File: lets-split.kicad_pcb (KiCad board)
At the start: 2 copper layers, 123.8 x 85.7 mm, 54 parts, among them J1 USB_C_Receptacle_USB2.0, SW1 Key_Tab, SW10 Key_D, SW11 Key_F, SW12 Key_G, SW13 Key_Shift, SW14 Key_Z, SW15 Key_X, SW16 Key_C, SW17 Key_V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

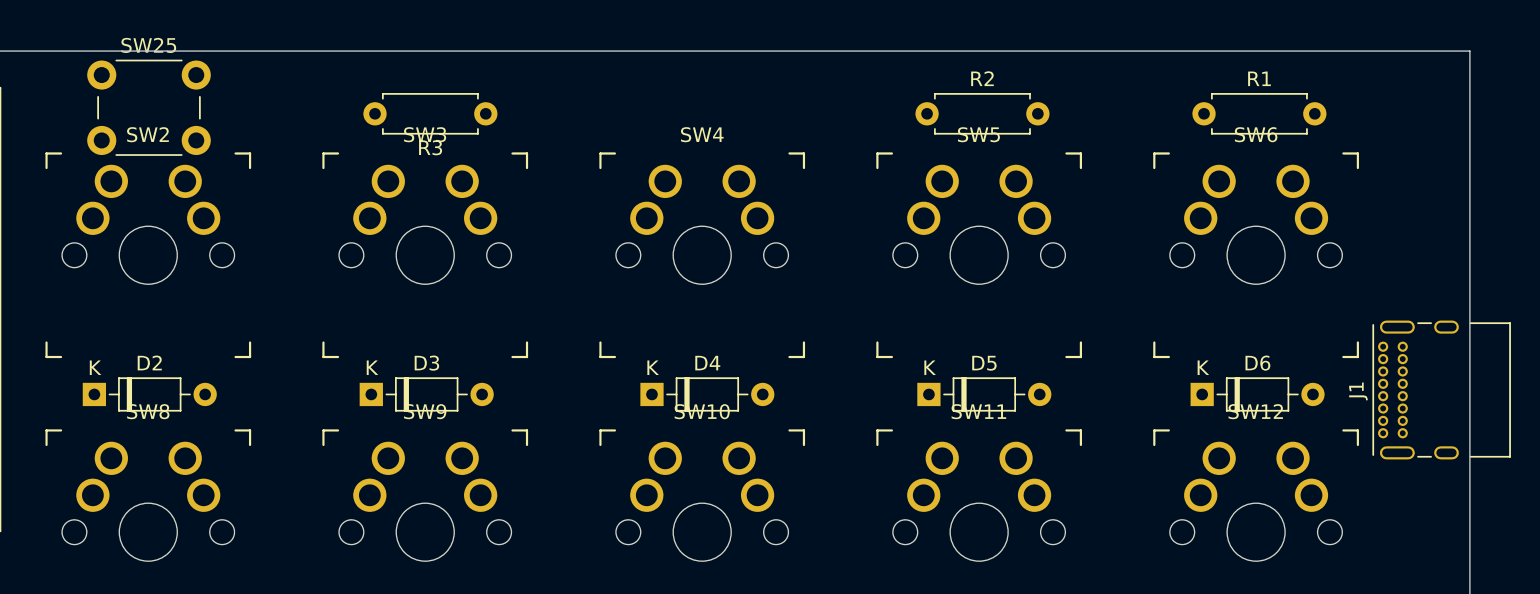
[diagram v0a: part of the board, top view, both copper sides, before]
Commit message: Fixed USB-C connector not passing inspection.
Added jumper to allow it to be mounted on either side of the board
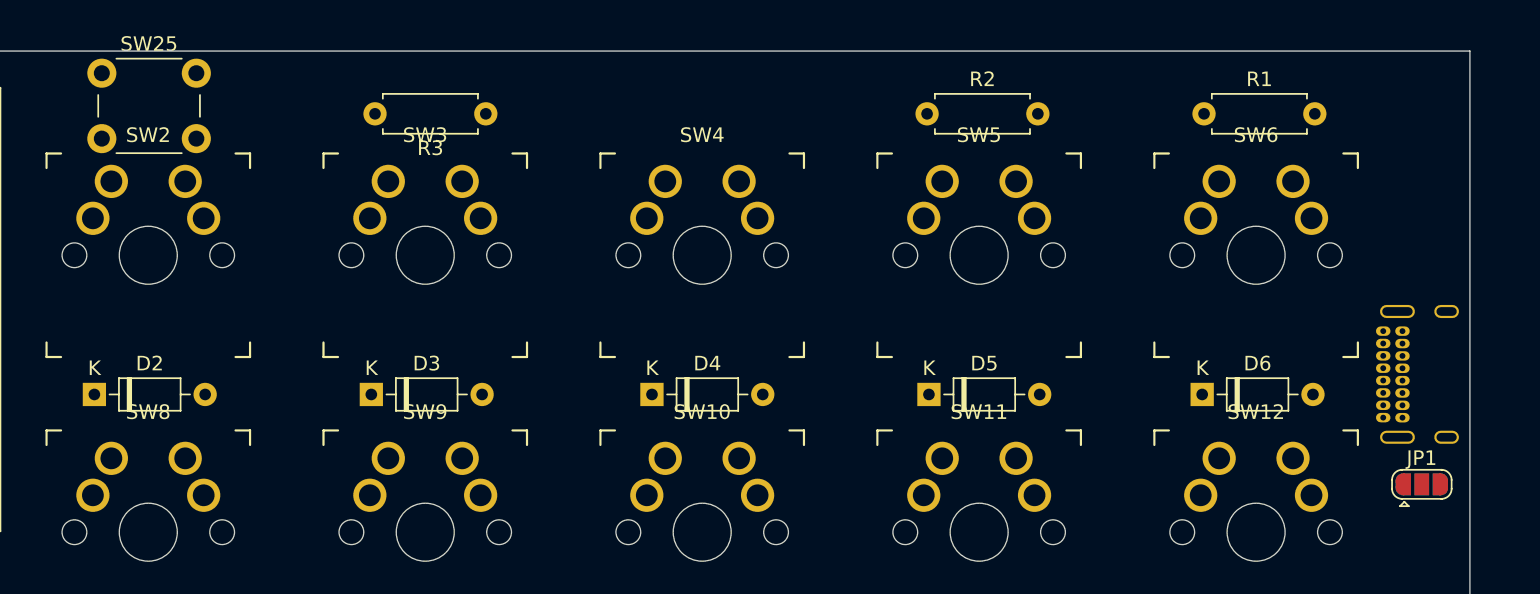
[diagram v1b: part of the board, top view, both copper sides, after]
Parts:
- added JP1: Jack Reversed Jumper, Jumper:SolderJumper-3_P1.3mm_Open_RoundedPad1.0x1.5mm, F.Cu at (196.7, 80.0)
- added JP2: Jack Obversed Jumper, Jumper:SolderJumper-3_P1.3mm_Open_RoundedPad1.0x1.5mm, B.Cu at (196.7, 80.0)
- J1: footprint Connector_USB:USB_C_Receptacle_GCT_USB4085 -> custom-footprints:USB_C_GCT_USB4085; moved to B.Cu
- moved J1 7.33 mm to (200.2, 72.4), turned to 270 degrees
- moved SW25 0.13 mm to (105.9, 51.7)
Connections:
- J1 pad B8: Net-(J1-PadA8) -> Net-(J1-PadB8)
- R3 pad 1: Net-(J1-PadA8) -> Net-(JP1-Pad1)

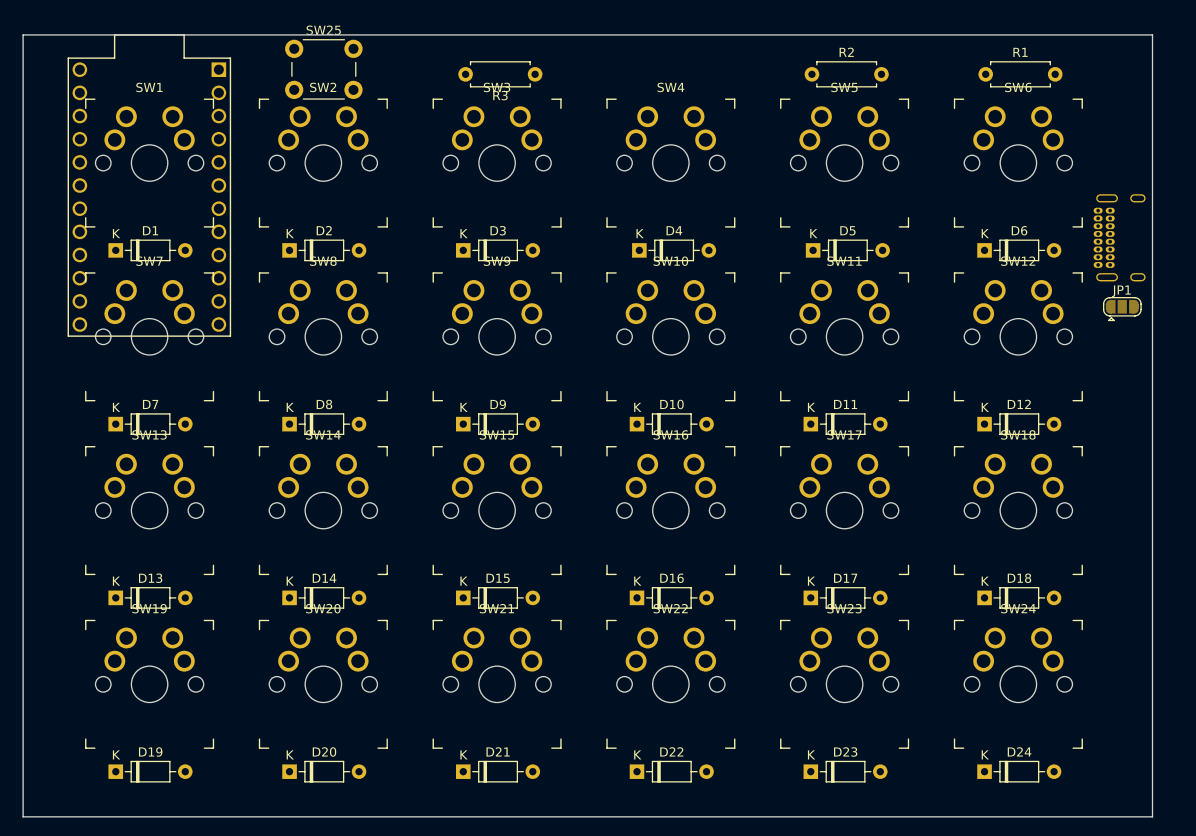
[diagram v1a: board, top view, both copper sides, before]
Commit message: PCB traces laid. Fixed labels on columns on schematic.
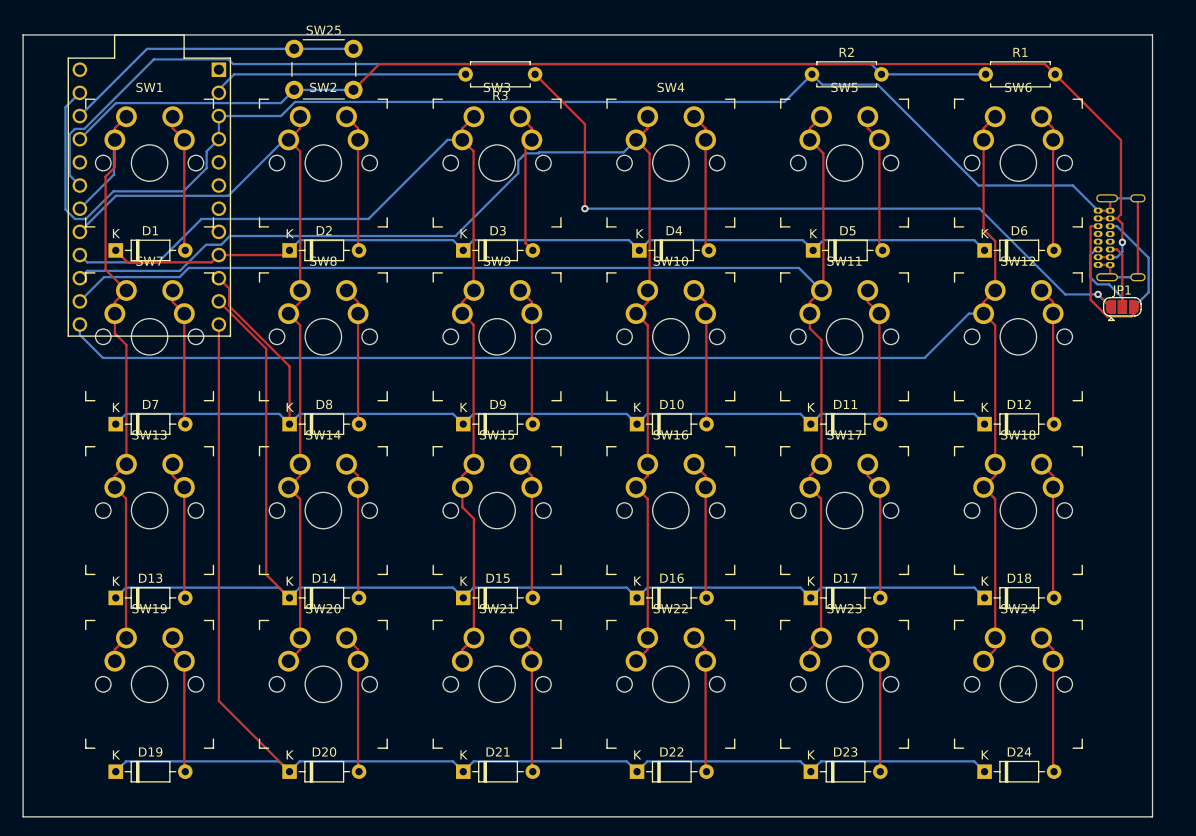
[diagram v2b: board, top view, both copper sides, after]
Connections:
- U1 pad 14: Col6 -> Col5
- U1 pad 15: Col6 -> Col4
- U1 pad 16: Col6 -> Col3
- U1 pad 17: Col6 -> Col2
- U1 pad 18: Col6 -> Col1
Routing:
- net Col6: track 0.00 -> 166.7 mm
- net GND: track 0.00 -> 163.5 mm
- net Row4: track 0.00 -> 152.1 mm
- net Col5: track 0.00 -> 147.4 mm
- net VCC: track 0.00 -> 138.7 mm, vias 0 -> 1
- net Row3: track 0.00 -> 135.6 mm
- net Col4: track 0.00 -> 131.6 mm
- net Row2: track 0.00 -> 119.1 mm
- net Col3: track 0.00 -> 111.2 mm
- net HalfSelector: track 0.00 -> 110.6 mm
- net Row1: track 0.00 -> 100.1 mm
- net Col2: track 0.00 -> 90.4 mm
- net Net-(JP1-Pad1): track 0.00 -> 81.0 mm, vias 0 -> 2
- net Col1: track 0.00 -> 73.4 mm
- net Reset: track 0.00 -> 33.1 mm
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
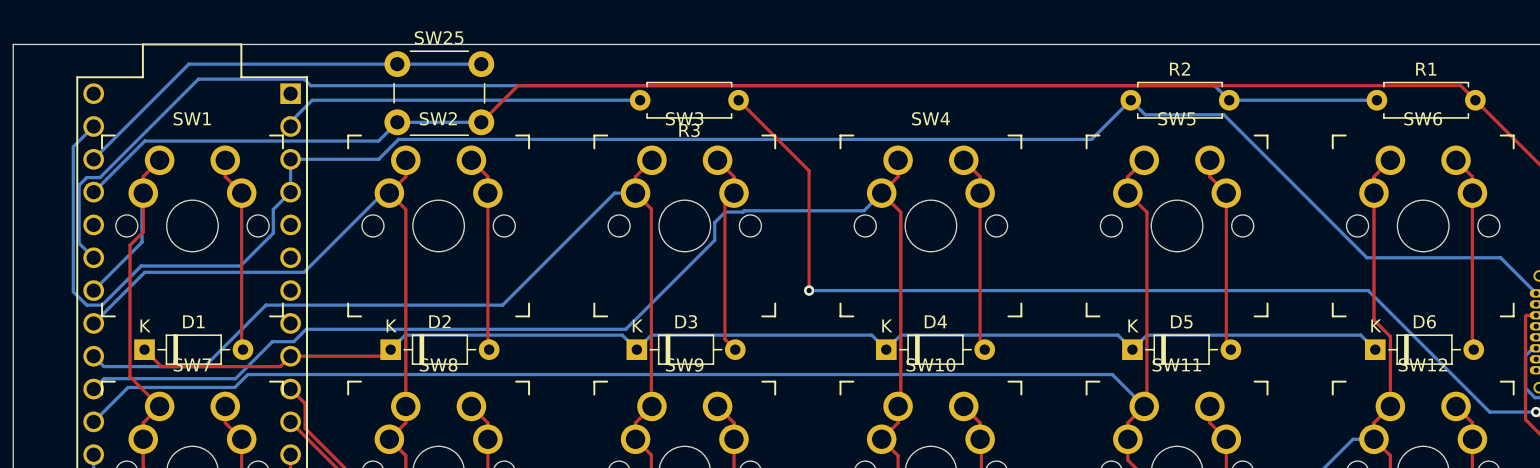
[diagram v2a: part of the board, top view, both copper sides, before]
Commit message: corrected reset button to go to gnd
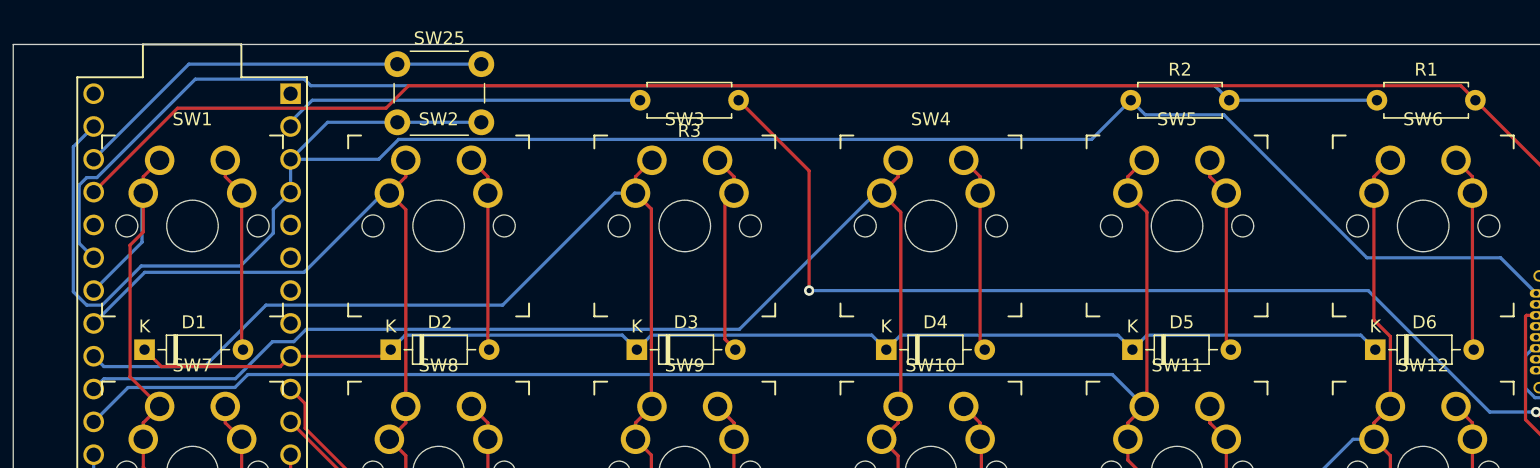
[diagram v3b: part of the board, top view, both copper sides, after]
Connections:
- SW25 pad 2: VCC -> GND
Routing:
- net GND: track 163.5 -> 179.4 mm
- net Col4: track 131.6 -> 130.8 mm

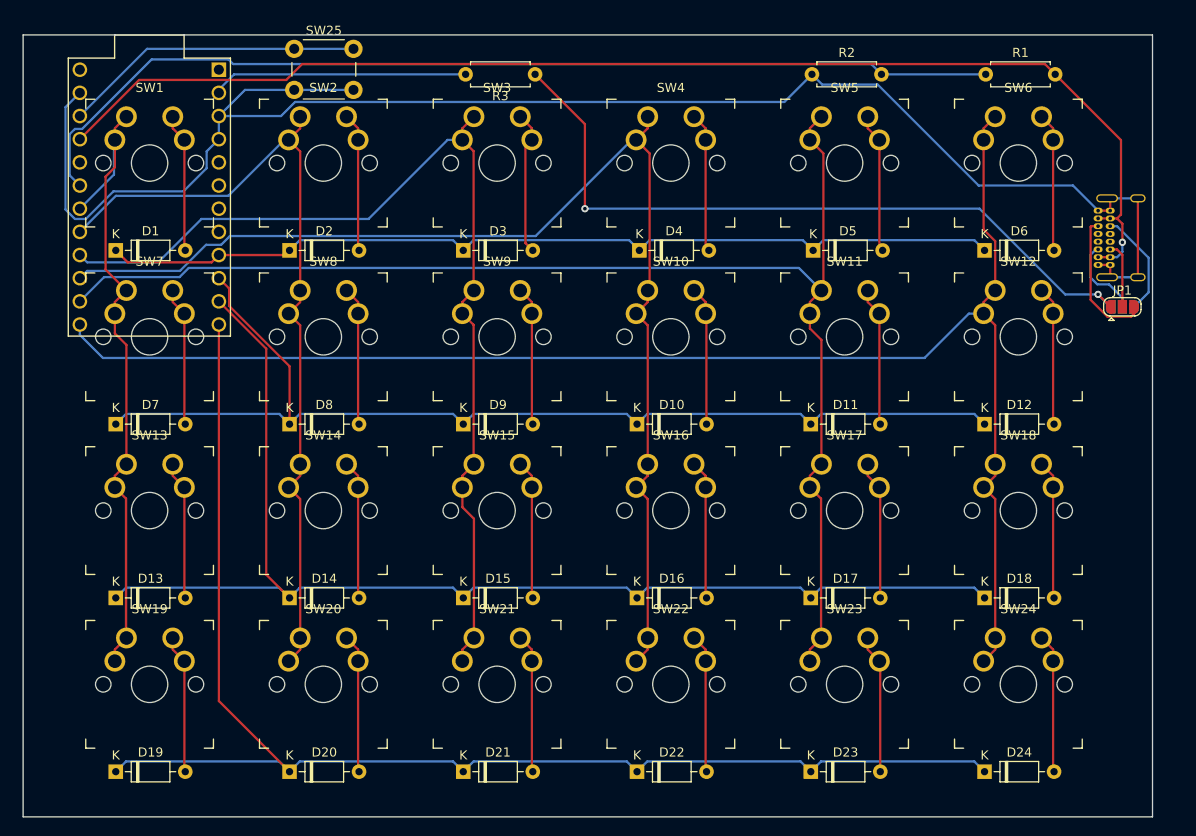
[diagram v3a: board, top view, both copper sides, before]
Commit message: Added ground planes
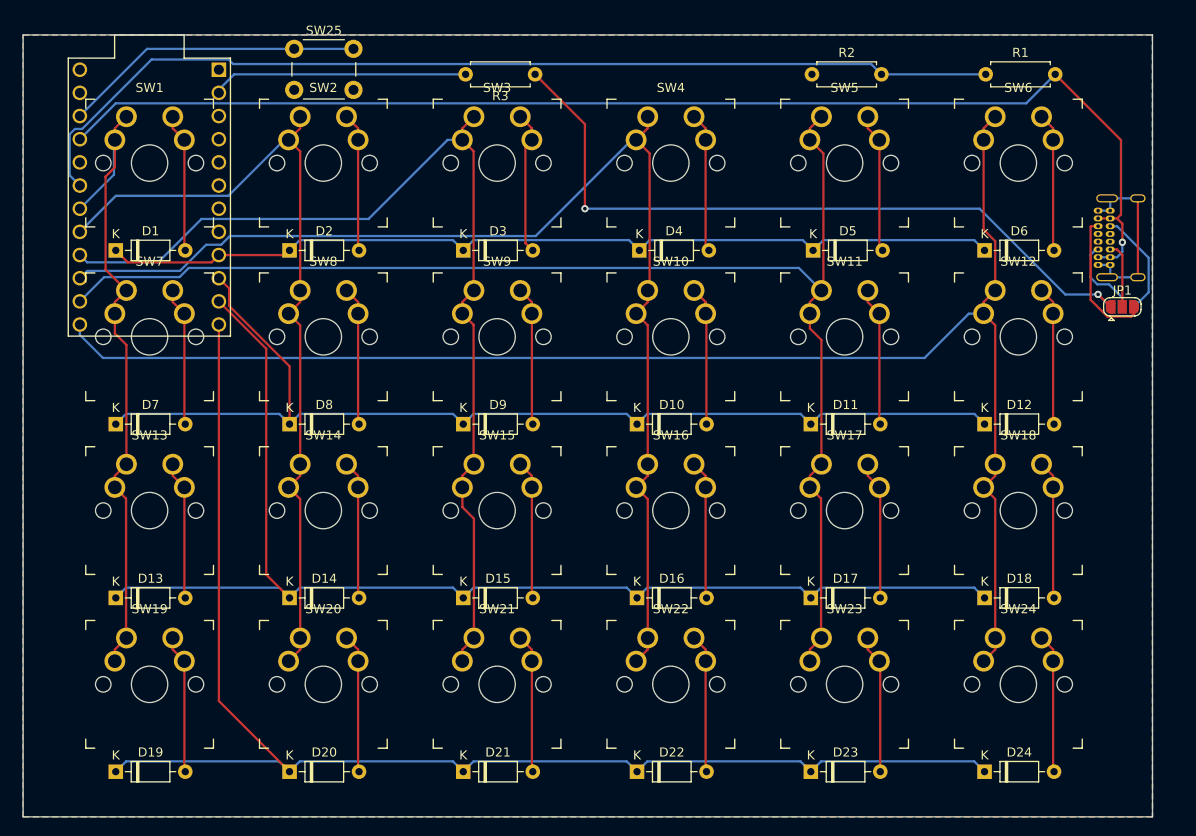
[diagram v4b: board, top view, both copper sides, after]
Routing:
- net GND: track 179.4 -> 22.0 mm
- net VCC: track 138.7 -> 137.7 mm
- added copper zone on B.Cu, net GND
- added copper zone on F.Cu, net GND

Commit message: added screw holes, tweaked board edge positions
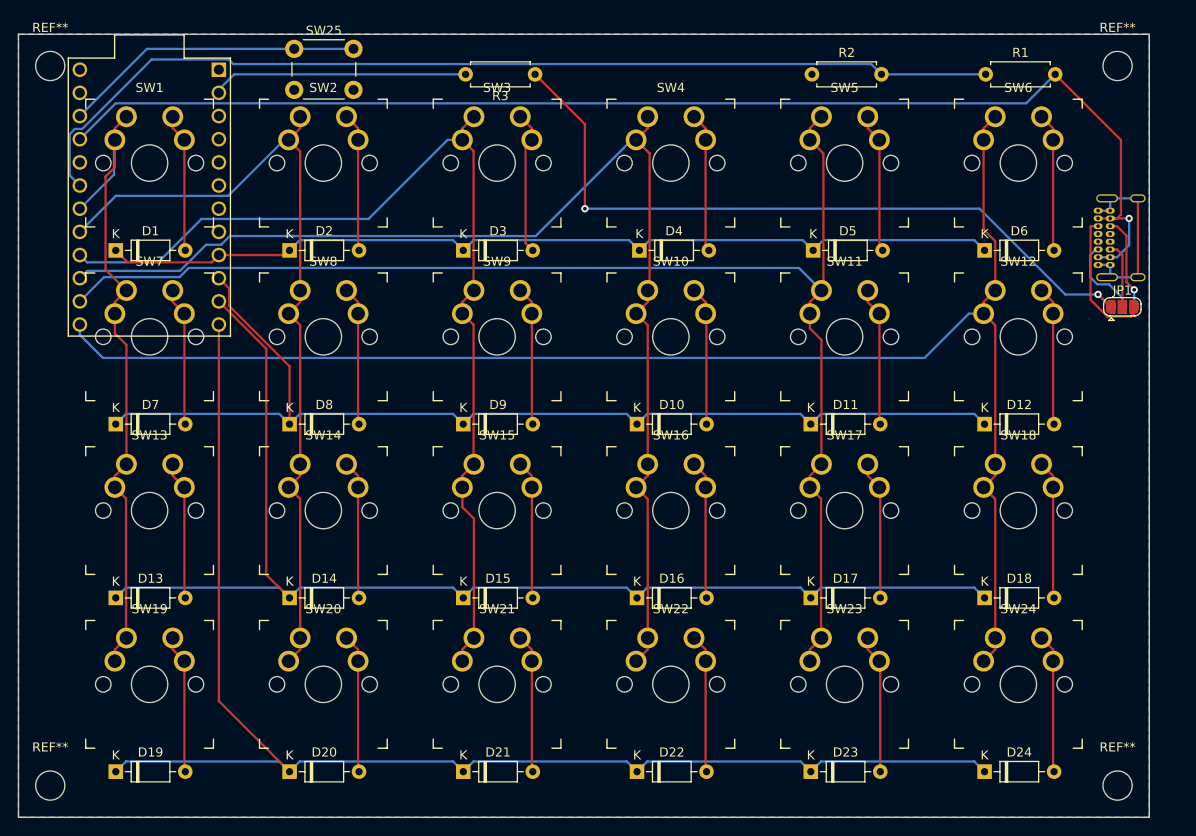
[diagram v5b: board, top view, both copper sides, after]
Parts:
- added REF**: MountingHole_3.2mm_M3, MountingHole:MountingHole_3.2mm_M3, F.Cu at (79.2, 132.5)
- added REF**: MountingHole_3.2mm_M3, MountingHole:MountingHole_3.2mm_M3, F.Cu at (79.2, 53.6)
- added REF**: MountingHole_3.2mm_M3, MountingHole:MountingHole_3.2mm_M3, F.Cu at (196.2, 132.5)
- added REF**: MountingHole_3.2mm_M3, MountingHole:MountingHole_3.2mm_M3, F.Cu at (196.2, 53.6)
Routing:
- net VCC: track 137.7 -> 139.9 mm
- net Net-(J1-PadB8): track 11.7 -> 10.4 mm, vias 0 -> 1
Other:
- board size 123.8 x 85.7 mm -> 124 x 85.9 mm

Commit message: Incorporated Kliment's feedback
Moved traces apart from everything
Removed one via
moved vias from under USB connector
Rounded corners
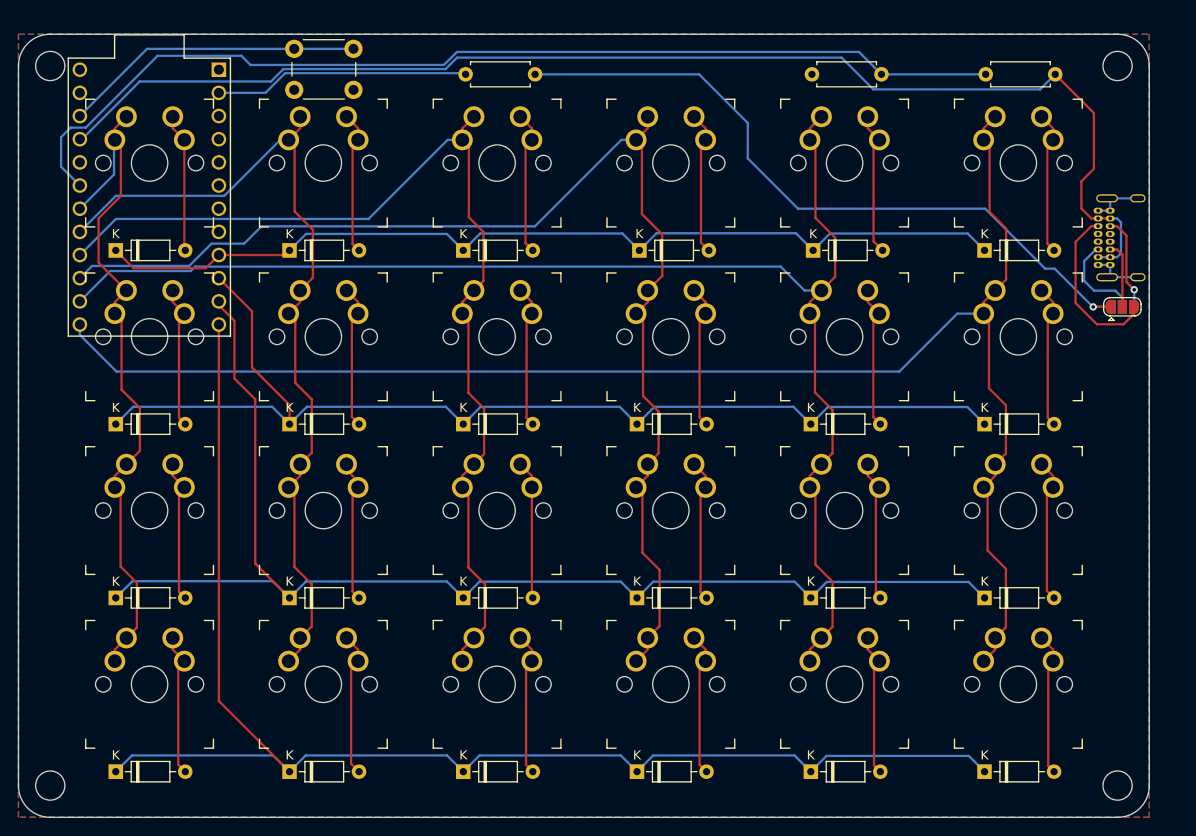
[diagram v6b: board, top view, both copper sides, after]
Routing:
- net GND: track 22.0 -> 13.4 mm
- net Col6: track 166.7 -> 170.8 mm
- net Col1: track 73.4 -> 76.7 mm
- net Col2: track 90.4 -> 93.7 mm
- net Net-(J1-PadA5): track 15.3 -> 18.5 mm
- net Col4: track 130.8 -> 134.0 mm
- net Row2: track 119.1 -> 122.3 mm
- net Col5: track 147.4 -> 150.6 mm
- net Net-(JP1-Pad1): track 81.0 -> 77.8 mm, vias 2 -> 1
- net Row1: track 100.1 -> 103.0 mm
- net Row3: track 135.6 -> 138.4 mm
- net Row4: track 152.1 -> 154.8 mm
- net HalfSelector: track 110.6 -> 113.3 mm
- net Col3: track 111.2 -> 113.3 mm
- net Net-(J1-PadA8): track 8.97 -> 10.2 mm
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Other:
- outline, holes or cut-outs redrawn

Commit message: added labels for jumpers and resistors
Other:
- board text added: "Left"
- board text added: "Right"
- board text added: "USB on far side"
